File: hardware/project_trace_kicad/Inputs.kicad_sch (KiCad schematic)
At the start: 22 parts, among them J101 Conn_Coaxial, J102 Conn_Coaxial, U101 AD8421, U102 AQW280SX, U103 AQW280SX, U201 ADA4807-1, U202 DAC81401

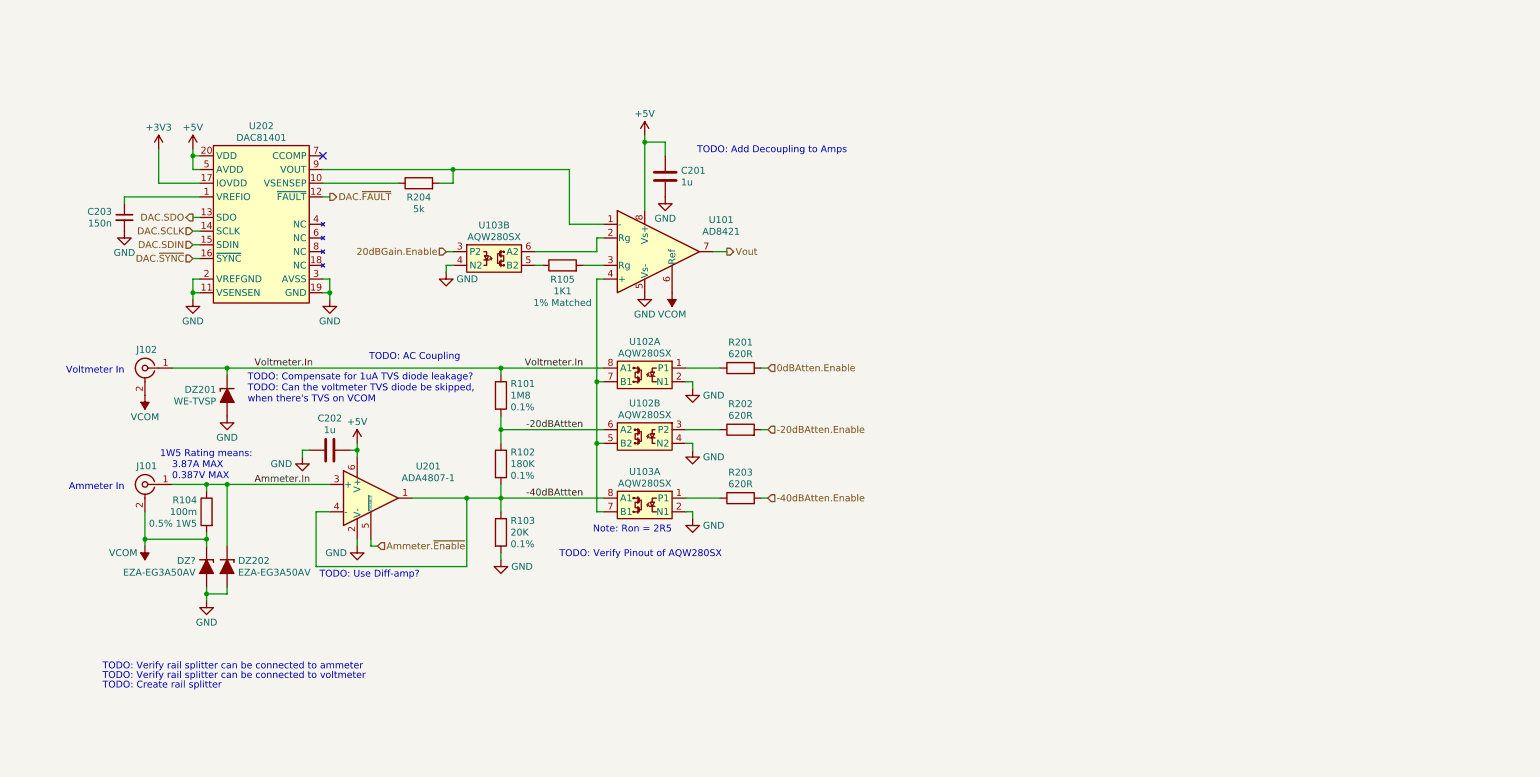
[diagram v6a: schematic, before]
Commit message: Add Decoupling, Fix Bugs
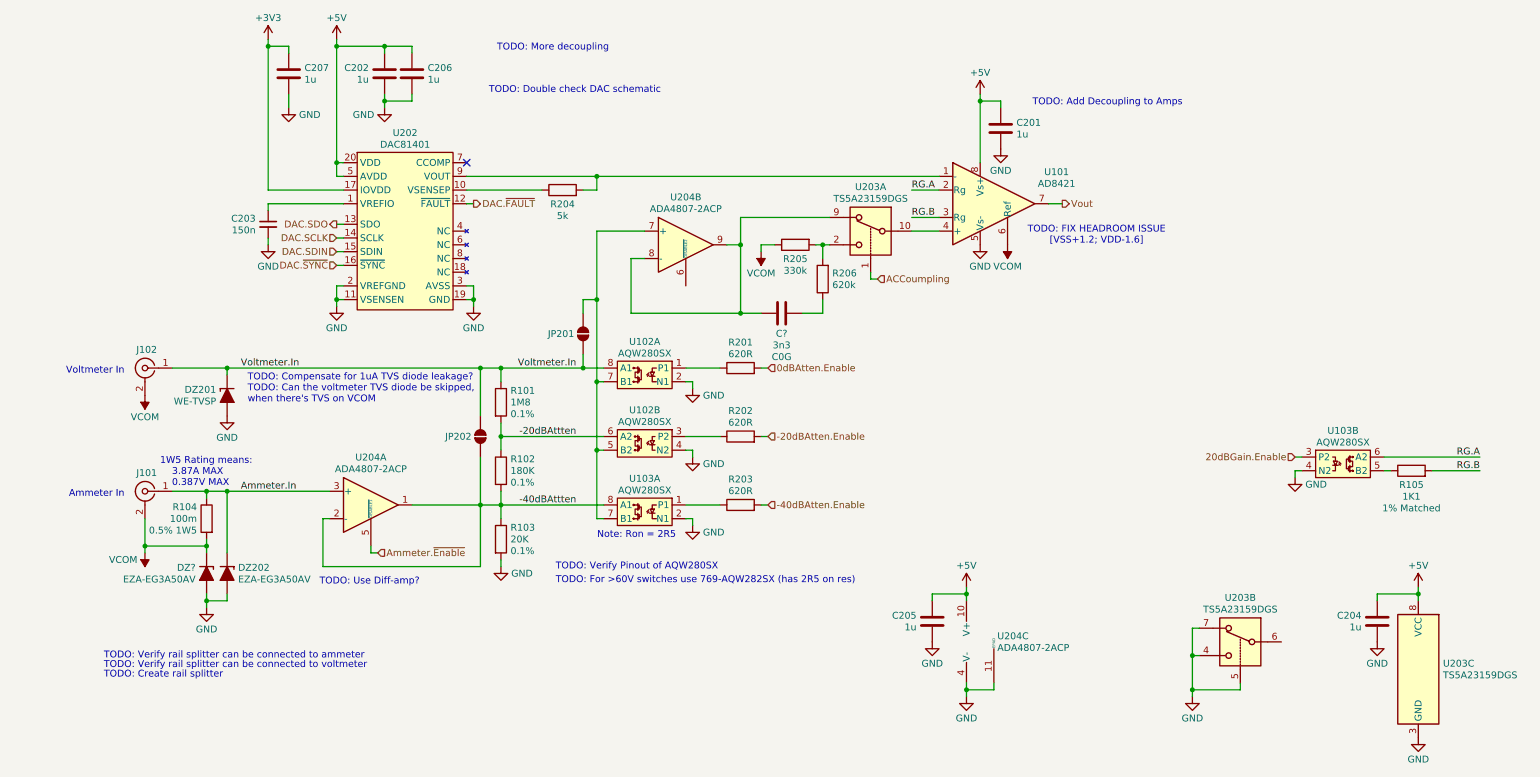
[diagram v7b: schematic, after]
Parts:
- removed U201: ADA4807-1, Package_TO_SOT_SMD:SOT-363_SC-70-6_Handsoldering, symbol Amplifier_Operational:ADA4807-1
- added C204, C205, C206, C207: 1u, symbol Device:C
- added C?: 3n3, symbol Device:C
- added JP201, JP202: SolderJumper_2_Open, symbol Jumper:SolderJumper_2_Open
- added R205: 330k, Resistor_SMD:R_0603_1608Metric_Pad0.98x0.95mm_HandSolder, symbol Device:R
- added R206: 620k, Resistor_SMD:R_0603_1608Metric_Pad0.98x0.95mm_HandSolder, symbol Device:R
- added U203: TS5A23159DGS, Package_SO:VSSOP-10_3x3mm_P0.5mm, symbol Analog_Switch:TS5A23159DGS
- added U204: ADA4807-2ACP, Package_CSP:LFCSP-WD-10-1EP_3x3mm_P0.5mm_EP1.64x2.38mm, symbol Amplifier_Operational:ADA4807-2ACP
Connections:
- net +3V3: now also C207.1
- net +5V: now also C202.1, C204.1, C205.1, C206.1, U203.8 (VCC), U204.10 (V+); no longer C202.2
- net -40dBAttten: now also JP202.1 (A), U204.1, U204.2 (-)
- net Ammeter.In: now also U204.3 (+)
- net Ammeter.~{Enable}: now also U204.5 (~{DISABLE1})
- net GND: now also C202.2, C204.2, C205.2, C206.2, C207.2, U203.3 (GND), U203.4, U203.5, U203.7, U204.11 (EPAD), U204.4 (V-); no longer C202.1
- net VCOM: now also R205.1
- net Voltmeter.In: now also JP201.1 (A), JP202.2 (B)
- net RG.B: now reaches R105.2, U101.3 (Rg)
- net at U102.5 (B2), U102.7 (B1), U103.7 (B1): now also JP201.2 (B), U204.7 (+); no longer U101.4 (+)
- net RG.A: now reaches U101.2 (Rg), U103.6 (A2)
- new net: R205.2, R206.2, U203.2
- new net: C?.2, R206.1
- new net: C?.1, U203.9, U204.8 (-), U204.9
- new net: U101.4 (+), U203.10
- new net ACCoumpling: U203.1
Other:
- note added: "TODO: Double check DAC schematic"
- note added: "TODO: FIX HEADROOM ISSUE [VSS+1.2; VDD-1.6]"
- note added: "TODO: For >60V switches use 769-AQW282SX (has 2R5 on res)"
- note added: "TODO: More decoupling"
- note removed: "TODO: AC Coupling"
- moved on the sheet: C201, C203, DZ202, DZ?, J101, R101, R102, R103, R104, R105, R202, R203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

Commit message: Fix Mistakes, Reduce Scope, improve Flexibility
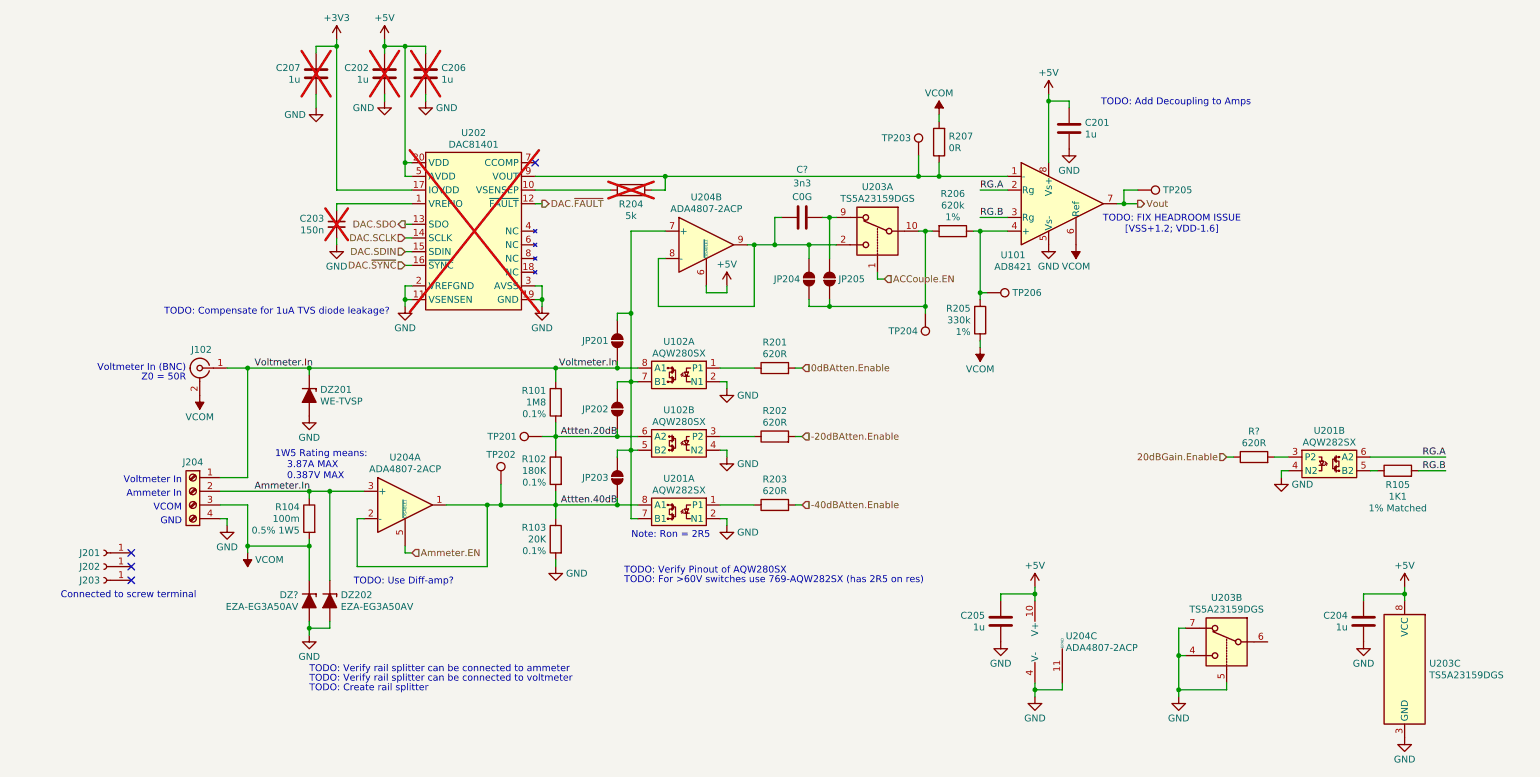
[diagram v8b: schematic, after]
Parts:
- removed J101: Conn_Coaxial, symbol Connector:Conn_Coaxial
- removed U103: AQW280SX, symbol ProjectTraceSymbols:AQW280SX
- added J201, J202, J203: Conn_01x01_Socket, symbol Connector:Conn_01x01_Socket
- added J204: Screw_Terminal_01x04, ProjectTraceFootprints:691210910004, symbol Connector:Screw_Terminal_01x04
- added JP203, JP204, JP205: SolderJumper_2_Open, symbol Jumper:SolderJumper_2_Open
- added R207: 0R, symbol Device:R
- added R?: 620R, Resistor_SMD:R_0603_1608Metric_Pad0.98x0.95mm_HandSolder, symbol Device:R
- added TP201, TP202, TP203, TP204, TP205, TP206: TestPoint, TestPoint:TestPoint_Pad_1.5x1.5mm, symbol Connector:TestPoint
- added U201: AQW282SX, ProjectTraceFootprints:AQW282SX, symbol ProjectTraceSymbols:AQW282SX
- C202, C203, C206, C207, R204, U202: now not fitted
- DZ201: DigikeyPN (none) -> 732-824540252TR-ND
- DZ202, DZ?: DigikeyPN (none) -> P13682CT-ND
- J102: footprint (none) -> ProjectTraceFootprints:BNC_Female_0731385003; DigikeyPN (none) -> WM14063-ND
- R104: DigikeyPN (none) -> 2019-SLW1TTER100DCT-ND
- R205, R206: Extra (none) -> 1%
- U102: DigikeyPN (none) -> 255-5713-1-ND
- U204: DigikeyPN (none) -> 505-ADA4807-2ARMZ-ND
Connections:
- net +5V: now also U204.6 (~{DISABLE2})
- net 20dBGain.Enable: now also R?.1
- net Ammeter.In: now also J204.2 (Pin_2)
- net GND: now also J204.4 (Pin_4), U201.2 (N1), U201.4 (N2)
- net RG.A: now also U201.6 (A2)
- net VCOM: now also J204.3 (Pin_3), R207.2
- net Voltmeter.In: now also J204.1 (Pin_1); no longer JP202.2 (B)
- net Vout: now also TP205.1
- net at R204.2, U101.1 (-), U202.9 (VOUT): now also R207.1, TP203.1
- net at R105.1: now also U201.5 (B2)
- net at R203.1: now also U201.1 (P1)
- net at JP201.2 (B), U102.5 (B2), U102.7 (B1)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: now also JP202.2 (B), JP203.2 (B), U201.7 (B1)
- net at R206.1: now also R205.2, U101.4 (+), TP206.1; no longer C?.2
- net at C?.1, U204.8 (-), U204.9: now also U203.2, JP204.1 (A); no longer U203.9
- net at U203.10: now also R206.2, JP204.2 (B), JP205.2 (B), TP204.1; no longer U101.4 (+)
- net -20dBAttten renamed Attten.20dB
- net Attten.20dB: now also JP202.1 (A), TP201.1
- net -40dBAttten renamed Attten.40dB
- net Attten.40dB: now also JP203.1 (A), TP202.1, U201.8 (A1); no longer JP202.1 (A)
- net ACCoumpling renamed ACCouple.EN
- net Ammeter.~{Enable} renamed Ammeter.EN
- new net: C?.2, JP205.1 (A), U203.9
- new net: R?.2, U201.3 (P2)
- no-connect marks 1 -> 4
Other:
- note added: "Connected to screw terminal"
- note added: "GND"
- note added: "VCOM"
- note added: "Voltmeter In (BNC)"
- note added: "Z0 = 50R"
- note removed: "TODO: Can the voltmeter TVS diode be skipped, when there's TVS on VCOM"
- note removed: "TODO: Double check DAC schematic"
- note removed: "TODO: More decoupling"
- moved on the sheet: C201, C204, C205, C?, DZ201, DZ202, DZ?, J102, JP201, JP202, R101, R102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
